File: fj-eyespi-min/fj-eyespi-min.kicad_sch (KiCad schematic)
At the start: 2 parts, among them J1 Conn_01x18_Socket, J2 Conn_02x16_Odd_Even

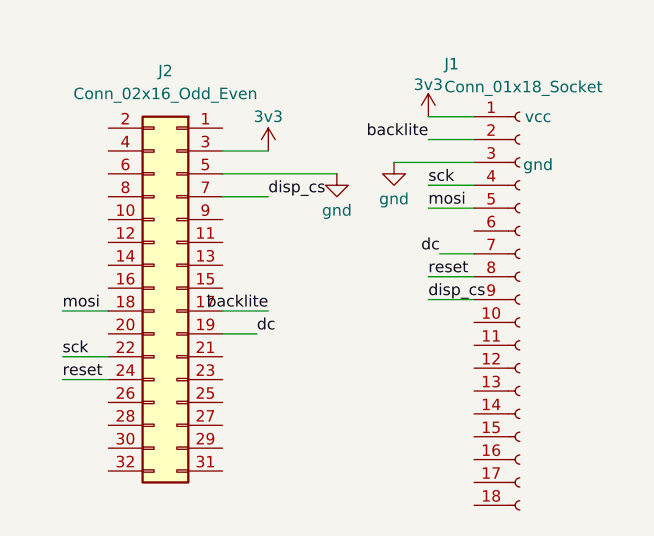
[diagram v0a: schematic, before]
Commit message: updated connector orientation
Flipped pin 1 and pin 18 direction by moving tracks for FFC connector
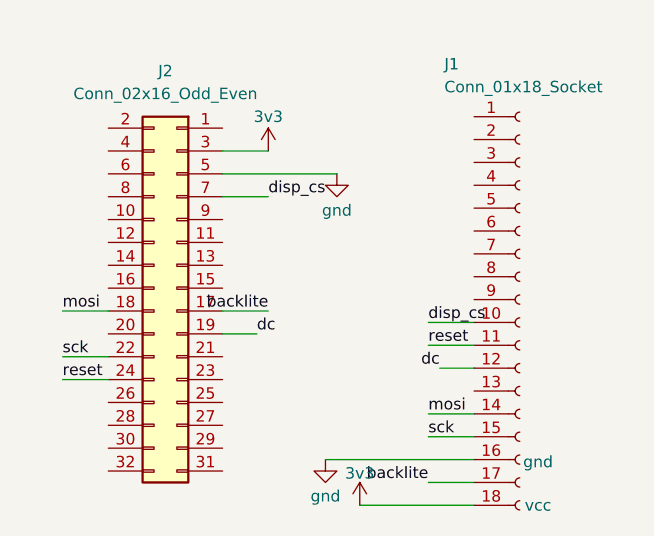
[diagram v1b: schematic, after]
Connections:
- net 3v3: now also J1.18 (Pin_18); no longer J1.1 (Pin_1)
- net backlite: now also J1.17 (Pin_17); no longer J1.2 (Pin_2)
- net dc: now also J1.12 (Pin_12); no longer J1.7 (Pin_7)
- net disp_cs: now also J1.10 (Pin_10); no longer J1.9 (Pin_9)
- net gnd: now also J1.16 (Pin_16); no longer J1.3 (Pin_3)
- net mosi: now also J1.14 (Pin_14); no longer J1.5 (Pin_5)
- net reset: now also J1.11 (Pin_11); no longer J1.8 (Pin_8)
- net sck: now also J1.15 (Pin_15); no longer J1.4 (Pin_4)
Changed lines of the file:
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@@
 	(text "gnd"
 		(exclude_from_sim no)
-		(at 191.262 70.358 0)
+		(at 191.262 103.378 0)
 		(effects
 			(font
@@
 	(text "vcc"
 		(exclude_from_sim no)
-		(at 191.262 65.024 0)
-		(effects
-			(font
-				(size 1.27 1.27)
-			)
-		)
-	)
-	(wire
-		(pts
-			(xy 179.07 74.93) (xy 184.15 74.93)
-		)
-		(stroke
-			(width 0)
-			(type default)
-		)
-	)
-	(wire
-		(pts
-			(xy 179.07 64.77) (xy 184.15 64.77)
-		)
-		(stroke
-			(width 0)
-			(type default)
-		)
-	)
-	(wire
-		(pts
-			(xy 184.15 72.39) (xy 179.07 72.39)
+		(at 191.262 108.204 0)
+		(effects
+			(font
+				(size 1.27 1.27)
+			)
+		)
+	)
+	(wire
+		(pts
+			(xy 179.07 97.79) (xy 184.15 97.79)
+		)
+		(stroke
+			(width 0)
+			(type default)
+		)
+	)
+	(wire
+		(pts
+			(xy 171.45 107.95) (xy 184.15 107.95)
+		)
+		(stroke
+			(width 0)
+			(type default)
+		)
+	)
+	(wire
+		(pts
+			(xy 184.15 100.33) (xy 179.07 100.33)
 		)
 		(stroke
@@
 	(wire
 		(pts
-			(xy 179.07 85.09) (xy 184.15 85.09)
-		)
-		(stroke
-			(width 0)
-			(type default)
-		)
-	)
-	(wire
-		(pts
-			(xy 184.15 69.85) (xy 175.26 69.85)
-		)
-		(stroke
-			(width 0)
-			(type default)
-		)
-	)
-	(wire
-		(pts
-			(xy 184.15 80.01) (xy 180.34 80.01)
+			(xy 179.07 87.63) (xy 184.15 87.63)
+		)
+		(stroke
+			(width 0)
+			(type default)
+		)
+	)
+	(wire
+		(pts
+			(xy 184.15 102.87) (xy 167.64 102.87)
+		)
+		(stroke
+			(width 0)
+			(type default)
+		)
+	)
+	(wire
+		(pts
+			(xy 184.15 92.71) (xy 180.34 92.71)
 		)
 		(stroke
@@
 	(wire
 		(pts
-			(xy 184.15 67.31) (xy 179.07 67.31)
+			(xy 184.15 105.41) (xy 179.07 105.41)
 		)
 		(stroke
@@
 	(wire
 		(pts
-			(xy 179.07 82.55) (xy 184.15 82.55)
+			(xy 179.07 90.17) (xy 184.15 90.17)
 		)
 		(stroke
@@
 	)
 	(label "sck"
-		(at 179.07 72.39 0)
+		(at 179.07 100.33 0)
 		(effects
 			(font
@@
 	)
 	(label "backlite"
-		(at 179.07 67.31 180)
+		(at 179.07 105.41 180)
 		(effects
 			(font
@@
 	)
 	(label "reset"
-		(at 179.07 82.55 0)
+		(at 179.07 90.17 0)
 		(effects
 			(font
@@
 	)
 	(label "dc"
-		(at 180.34 80.01 180)
+		(at 180.34 92.71 180)
 		(effects
 			(font
@@
 	)
 	(label "disp_cs"
-		(at 179.07 85.09 0)
+		(at 179.07 87.63 0)
 		(effects
 			(font
@@
 	)
 	(label "mosi"
-		(at 179.07 74.93 0)
+		(at 179.07 97.79 0)
 		(effects
 			(font
@@
 	(symbol
 		(lib_id "power:GND")
-		(at 175.26 69.85 0)
+		(at 167.64 102.87 0)
 		(unit 1)
 		(exclude_from_sim no)
@@
 		(dnp no)
 		(property "Reference" "#PWR04"
-			(at 175.26 76.2 0)
+			(at 167.64 109.22 0)
 			(effects
 				(font
@@
 		)
 		(property "Value" "gnd"
-			(at 175.26 73.914 0)
+			(at 167.64 106.934 0)
 			(effects
 				(font
@@
 		)
 		(property "Footprint" ""
-			(at 175.26 69.85 0)
+			(at 167.64 102.87 0)
 			(effects
 				(font
@@
 		)
 		(property "Datasheet" ""
-			(at 175.26 69.85 0)
+			(at 167.64 102.87 0)
 			(effects
 				(font
@@
 		)
 		(property "Description" "Power symbol creates a global label with name \"GND\" , ground"
-			(at 175.26 69.85 0)
+			(at 167.64 102.87 0)
 			(effects
 				(font
@@
 	(symbol
 		(lib_id "power:+3V3")
-		(at 179.07 64.77 0)
+		(at 171.45 107.95 0)
 		(unit 1)
 		(exclude_from_sim no)
@@
 		(dnp no)
 		(property "Reference" "#PWR02"
-			(at 179.07 68.58 0)
+			(at 171.45 111.76 0)
 			(effects
 				(font
@@
 		)
 		(property "Value" "3v3"
-			(at 179.07 61.214 0)
+			(at 171.45 104.394 0)
 			(effects
 				(font
@@
 		)
 		(property "Footprint" ""
-			(at 179.07 64.77 0)
+			(at 171.45 107.95 0)
 			(effects
 				(font
@@
 		)
 		(property "Datasheet" ""
-			(at 179.07 64.77 0)
+			(at 171.45 107.95 0)
 			(effects
 				(font
@@
 		)
 		(property "Description" "Power symbol creates a global label with name \"+3V3\""
-			(at 179.07 64.77 0)
-			(effects
-				(font
+			(at 171.45 107.95 0)
+			(effects
+				(font

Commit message: min new layout optimized trax
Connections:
- net 3v3: now also J2.29 (Pin_29); no longer J2.3 (Pin_3)
- net dc: now also J2.13 (Pin_13); no longer J2.19 (Pin_19)
- net gnd: now also J2.27 (Pin_27), J2.28 (Pin_28), J2.6 (Pin_6)
- net rst: now reaches J2.11 (Pin_11)
- net rst: now also J1.11 (Pin_11)
- net lite: now reaches J2.25 (Pin_25)
- net lite: now also J1.17 (Pin_17)
- net tcs: now reaches J2.9 (Pin_9)
- net tcs: now also J1.10 (Pin_10)
- net backlite: no longer names the net of J2.17 (Pin_17)
- net backlite: no longer J1.17 (Pin_17)
- net disp_cs: no longer names the net of J2.7 (Pin_7)
- net disp_cs: no longer J1.10 (Pin_10)
- net reset: no longer names the net of J2.24 (Pin_24)
- net reset: no longer J1.11 (Pin_11)
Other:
- moved on the sheet: J1
